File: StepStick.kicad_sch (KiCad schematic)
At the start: 3 parts

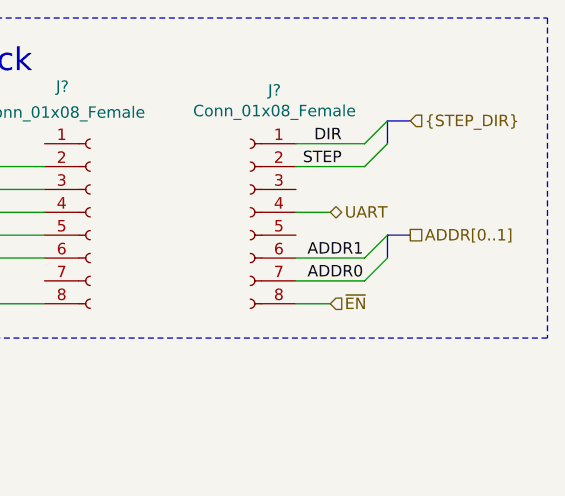
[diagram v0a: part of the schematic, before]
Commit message: Increase text size, redo bus labels
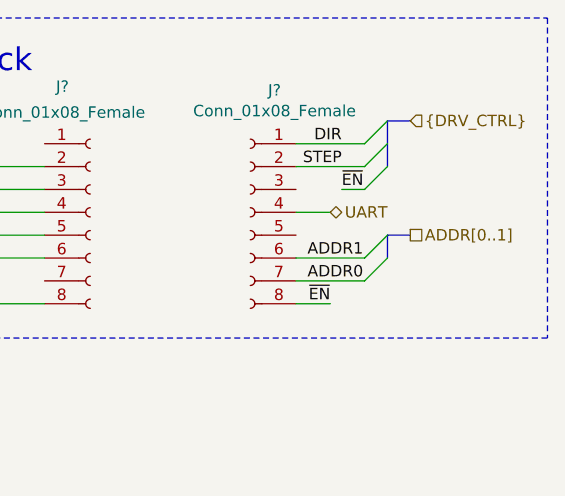
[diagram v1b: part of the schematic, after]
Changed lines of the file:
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@@
-(kicad_sch (version 20200608) (host eeschema "5.99.0-unknown-18ab3c4~101~ubuntu20.04.1")
+(kicad_sch (version 20200608) (host eeschema "5.99.0-unknown-e376750~101~ubuntu20.04.1")
   (page 4 11)
   (paper "A4")
@@
     (comment 1 "Drawn by: Cameron McQuinn")
   )
-  (bus_alias "STEP_DIR" (members "STEP" "DIR"))
+  (bus_alias "DRV_CTRL" (members "STEP" "DIR" "~EN"))
   (bus_entry (at 157.48 77.47) (size 2.54 -2.54))
   (bus_entry (at 157.48 80.01) (size 2.54 -2.54))
+  (bus_entry (at 157.48 82.55) (size 2.54 -2.54))
   (bus_entry (at 157.48 90.17) (size 2.54 -2.54))
   (bus_entry (at 157.48 92.71) (size 2.54 -2.54))
@@
     (stroke (width 0) (type solid) (color 0 0 0 0))
   )
-  (bus (pts (xy 160.02 74.93) (xy 162.56 74.93))
+  (wire (pts (xy 154.94 82.55) (xy 157.48 82.55))
     (stroke (width 0) (type solid) (color 0 0 0 0))
   )
-  (bus (pts (xy 160.02 77.47) (xy 160.02 74.93))
+  (bus (pts (xy 160.02 74.93) (xy 160.02 80.01))
+    (stroke (width 0) (type solid) (color 0 0 0 0))
+  )
+  (bus (pts (xy 160.02 74.93) (xy 162.56 74.93))
     (stroke (width 0) (type solid) (color 0 0 0 0))
   )
@@
     (effects (font (size 1.27 1.27)) (justify left bottom))
   )
+  (label "~EN" (at 153.67 95.25 180)
+    (effects (font (size 1.27 1.27)) (justify right bottom))
+  )
   (label "DIR" (at 154.94 77.47 180)
     (effects (font (size 1.27 1.27)) (justify right bottom))
@@
     (effects (font (size 1.27 1.27)) (justify right bottom))
   )
+  (label "~EN" (at 154.94 82.55 0)
+    (effects (font (size 1.27 1.27)) (justify left bottom))
+  )
   (hierarchical_label "UART" (shape bidirectional) (at 153.67 85.09 0)
     (effects (font (size 1.27 1.27)) (justify left))
   )
-  (hierarchical_label "~EN" (shape input) (at 153.67 95.25 0)
+  (hierarchical_label "{DRV_CTRL}" (shape input) (at 162.56 74.93 0)
     (effects (font (size 1.27 1.27)) (justify left))
   )
-  (hierarchical_label "{STEP_DIR}" (shape input) (at 162.56 74.93 0)
-    (effects (font (size 1.27 1.27)) (justify left))
-  )

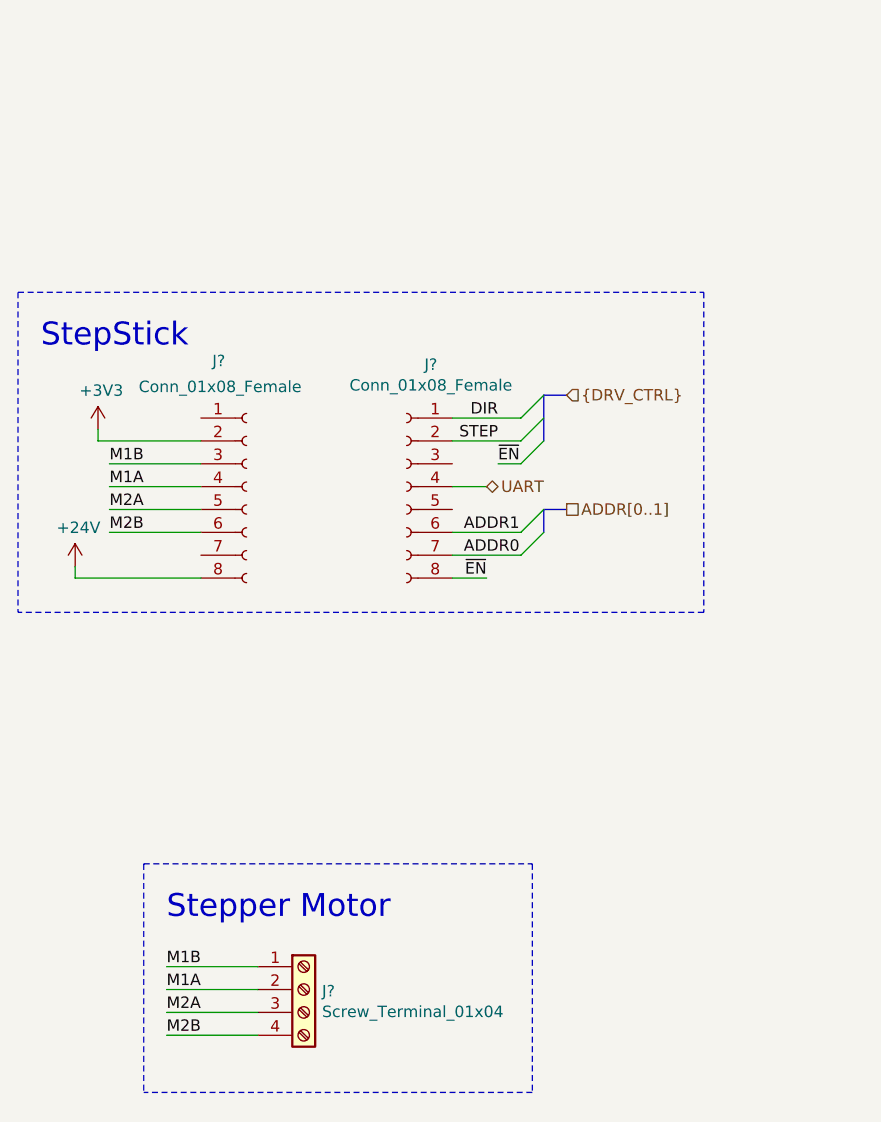
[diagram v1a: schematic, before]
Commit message: Configure driver chip address with jumpers
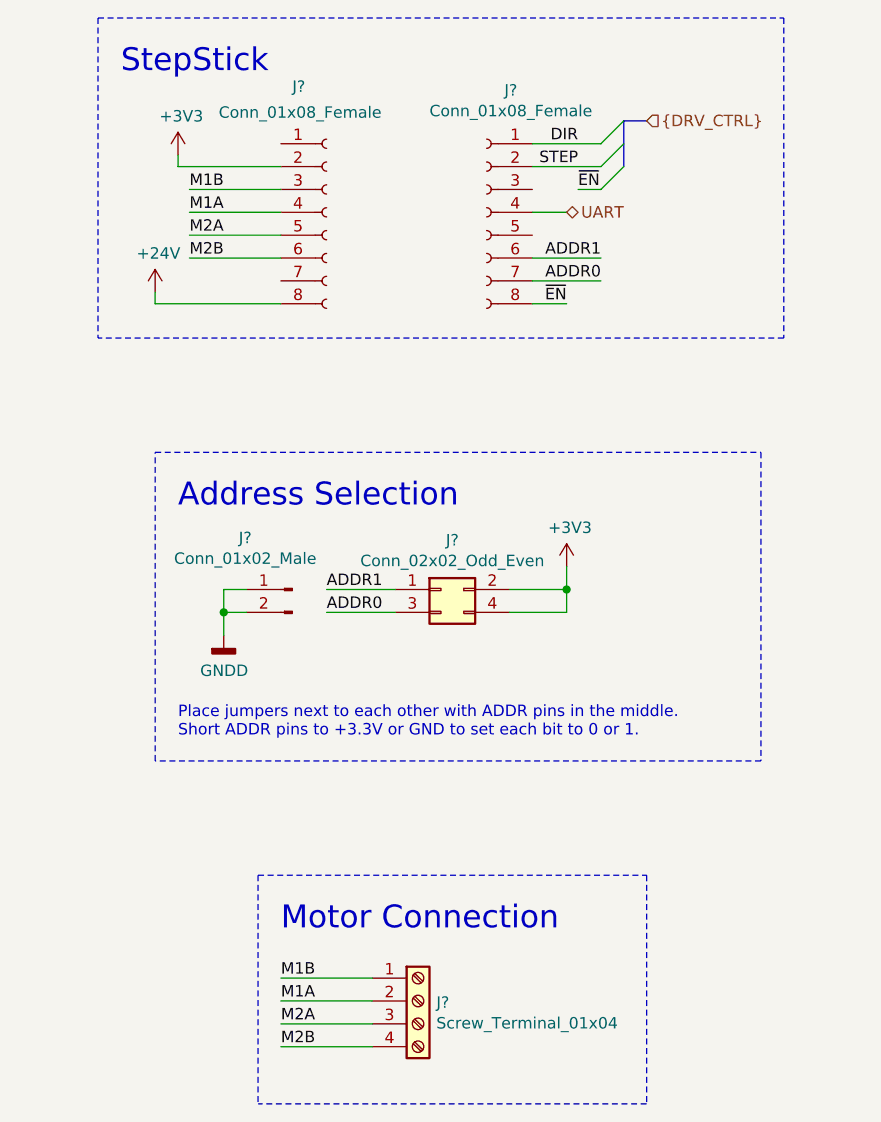
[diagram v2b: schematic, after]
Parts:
- added J?: Conn_01x02_Male, symbol Connector:Conn_01x02_Male
- added J?: Conn_02x02_Odd_Even, symbol Connector_Generic:Conn_02x02_Odd_Even
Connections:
- net +3V3: now also J?.2 (Pin_2), J?.4 (Pin_4)
- net ADDR0: now also J?.3 (Pin_3)
- net ADDR1: now also J?.1 (Pin_1)
- new net GNDD: J?.1 (Pin_1), J?.2 (Pin_2)
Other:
- note added: "Address Selection"
- note added: "Motor Connection"
- note added: "Place jumpers next to each other with ADDR pins in the middle. Short ADDR pins to +3.3V or GND to set each bit to 0 or 1."
- note removed: "Stepper Motor"
- moved on the sheet: J?

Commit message: Annotate schematic
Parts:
- gave numbers to parts that had none: 5
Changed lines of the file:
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@@
-(kicad_sch (version 20200618) (host eeschema "5.99.0-unknown-1463dd1~101~ubuntu20.04.1")
+(kicad_sch (version 20200618) (host eeschema "5.99.0-unknown-77313e4~101~ubuntu20.04.1")
   (page 1 13)
-  (paper "A4")
+  (paper "B")
   (title_block
     (title "StepStick")
@@
   (symbol (lib_id "power:+24V") (at 116.84 63.5 0)
     (in_bom yes) (on_board yes)
-    (property "Reference" "#PWR?" (id 0) (at 116.84 67.31 0)
+    (property "Reference" "#PWR01301" (id 0) (at 116.84 67.31 0)
       (effects (font (size 1.27 1.27)) hide)
     )
@@
   (symbol (lib_id "power:+3V3") (at 119.38 48.26 0)
     (in_bom yes) (on_board yes)
-    (property "Reference" "#PWR?" (id 0) (at 119.38 52.07 0)
+    (property "Reference" "#PWR01302" (id 0) (at 119.38 52.07 0)
       (effects (font (size 1.27 1.27)) hide)
     )
@@
   (symbol (lib_id "power:+3V3") (at 162.56 93.98 0)
     (in_bom yes) (on_board yes)
-    (property "Reference" "#PWR?" (id 0) (at 162.56 97.79 0)
+    (property "Reference" "#PWR01304" (id 0) (at 162.56 97.79 0)
       (effects (font (size 1.27 1.27)) hide)
     )
@@
   (symbol (lib_id "power:GNDD") (at 124.46 101.6 0)
     (in_bom yes) (on_board yes)
-    (property "Reference" "#PWR?" (id 0) (at 124.46 107.95 0)
+    (property "Reference" "#PWR01303" (id 0) (at 124.46 107.95 0)
       (effects (font (size 1.27 1.27)) hide)
     )
@@
   (symbol (lib_id "Connector:Conn_01x02_Male") (at 132.08 96.52 0) (mirror y)
     (in_bom yes) (on_board yes)
-    (property "Reference" "J?" (id 0) (at 126.8476 90.7858 0))
+    (property "Reference" "J1301" (id 0) (at 126.8476 90.7858 0))
     (property "Value" "Conn_01x02_Male" (id 1) (at 126.8476 93.0845 0))
     (property "Footprint" "" (id 2) (at 132.08 96.52 0)
@@
   (symbol (lib_id "Connector:Screw_Terminal_01x04") (at 146.05 142.24 0)
     (in_bom yes) (on_board yes)
-    (property "Reference" "J?" (id 0) (at 148.0821 142.4114 0)
+    (property "Reference" "J1303" (id 0) (at 148.0821 142.4114 0)
       (effects (font (size 1.27 1.27)) (justify left))
     )
@@
   (symbol (lib_id "Connector_Generic:Conn_02x02_Odd_Even") (at 148.59 96.52 0)
     (in_bom yes) (on_board yes)
-    (property "Reference" "J?" (id 0) (at 149.86 91.0398 0))
+    (property "Reference" "J1304" (id 0) (at 149.86 91.0398 0))
     (property "Value" "Conn_02x02_Odd_Even" (id 1) (at 149.86 93.3385 0))
     (property "Footprint" "" (id 2) (at 148.59 96.52 0)
@@
   (symbol (lib_id "Connector:Conn_01x08_Female") (at 135.89 54.61 0)
     (in_bom yes) (on_board yes)
-    (property "Reference" "J?" (id 0) (at 132.08 40.64 0)
+    (property "Reference" "J1302" (id 0) (at 132.08 40.64 0)
       (effects (font (size 1.27 1.27)) (justify left))
     )
@@
   (symbol (lib_id "Connector:Conn_01x08_Female") (at 153.67 54.61 0) (mirror y)
     (in_bom yes) (on_board yes)
-    (property "Reference" "J?" (id 0) (at 156.3624 41.0526 0))
+    (property "Reference" "J1305" (id 0) (at 156.3624 41.0526 0))
     (property "Value" "Conn_01x08_Female" (id 1) (at 156.3624 43.3513 0))
     (property "Footprint" "" (id 2) (at 153.67 54.61 0)

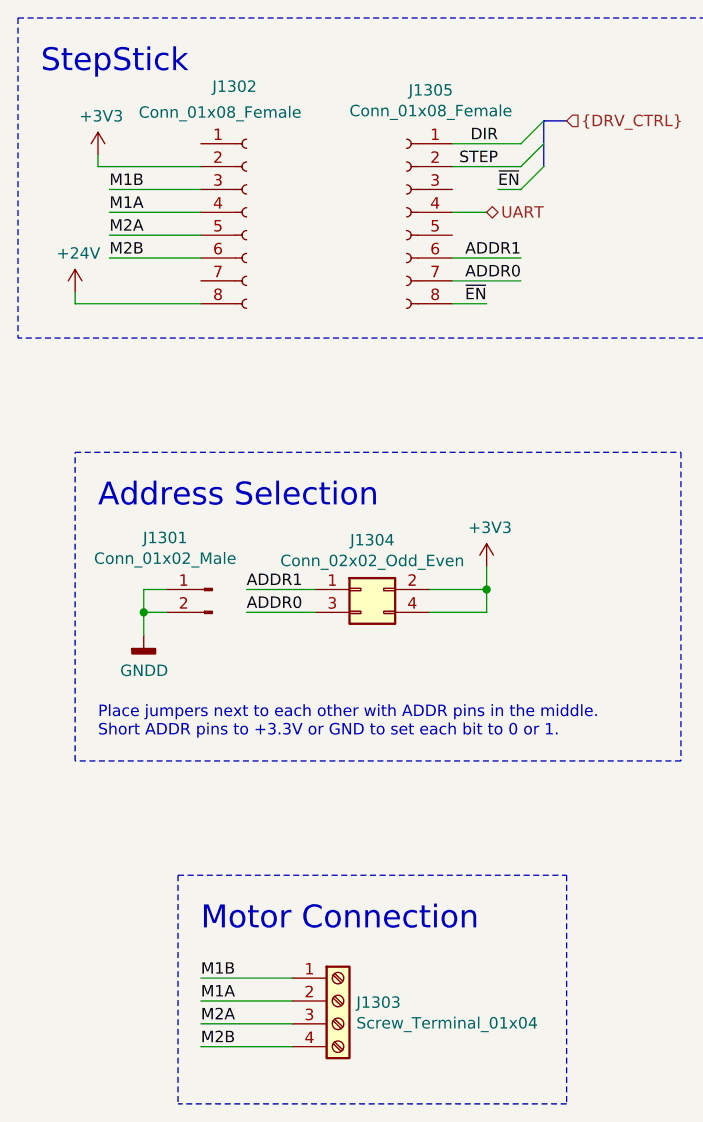
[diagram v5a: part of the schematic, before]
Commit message: Add ULPI USB PHY
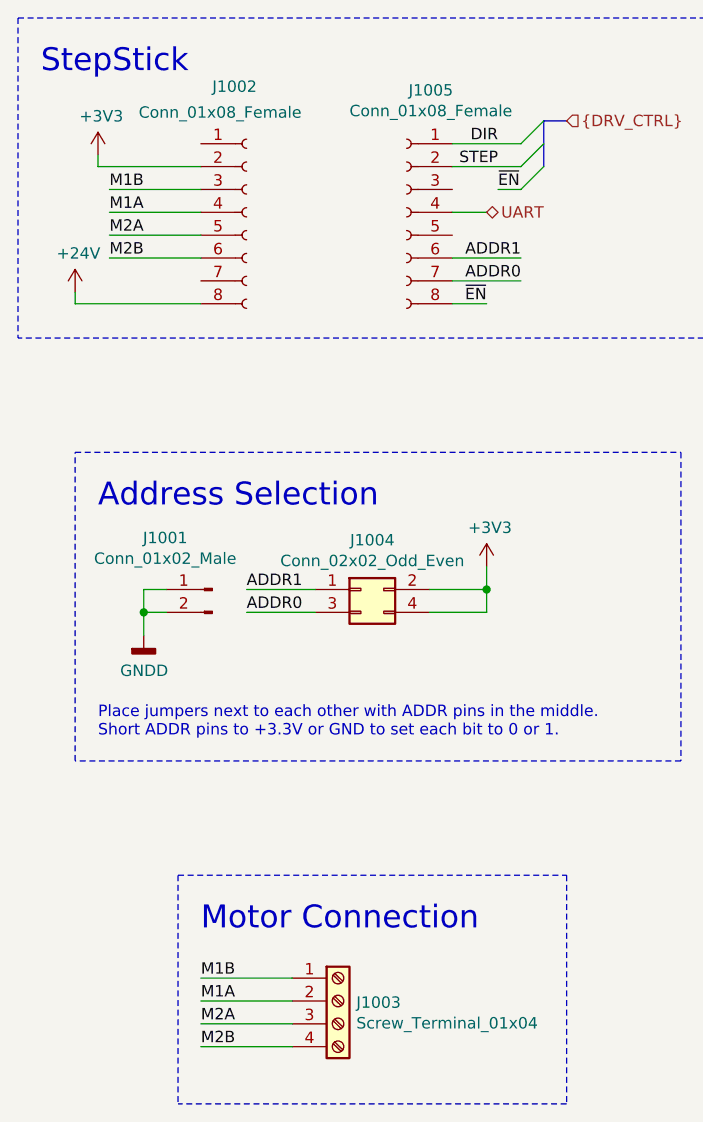
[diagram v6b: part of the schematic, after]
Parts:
- renumbered J1301 to J1001, J1302 to J1002, J1303 to J1003, J1304 to J1004, J1305 to J1005
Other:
- title: StepStick -> StepStick Interface
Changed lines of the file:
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@@
 (kicad_sch (version 20200618) (host eeschema "5.99.0-unknown-77313e4~101~ubuntu20.04.1")
-  (page 1 13)
+  (page 11 14)
   (paper "B")
   (title_block
-    (title "StepStick")
+    (title "StepStick Interface")
     (date "2020-06-24")
     (rev "1.0")
@@
   (symbol (lib_id "power:+24V") (at 116.84 63.5 0)
     (in_bom yes) (on_board yes)
-    (property "Reference" "#PWR01301" (id 0) (at 116.84 67.31 0)
+    (property "Reference" "#PWR01001" (id 0) (at 116.84 67.31 0)
       (effects (font (size 1.27 1.27)) hide)
     )
@@
   (symbol (lib_id "power:+3V3") (at 119.38 48.26 0)
     (in_bom yes) (on_board yes)
-    (property "Reference" "#PWR01302" (id 0) (at 119.38 52.07 0)
+    (property "Reference" "#PWR01002" (id 0) (at 119.38 52.07 0)
       (effects (font (size 1.27 1.27)) hide)
     )
@@
   (symbol (lib_id "power:+3V3") (at 162.56 93.98 0)
     (in_bom yes) (on_board yes)
-    (property "Reference" "#PWR01304" (id 0) (at 162.56 97.79 0)
+    (property "Reference" "#PWR01004" (id 0) (at 162.56 97.79 0)
       (effects (font (size 1.27 1.27)) hide)
     )
@@
   (symbol (lib_id "power:GNDD") (at 124.46 101.6 0)
     (in_bom yes) (on_board yes)
-    (property "Reference" "#PWR01303" (id 0) (at 124.46 107.95 0)
+    (property "Reference" "#PWR01003" (id 0) (at 124.46 107.95 0)
       (effects (font (size 1.27 1.27)) hide)
     )
@@
   (symbol (lib_id "Connector:Conn_01x02_Male") (at 132.08 96.52 0) (mirror y)
     (in_bom yes) (on_board yes)
-    (property "Reference" "J1301" (id 0) (at 126.8476 90.7858 0))
+    (property "Reference" "J1001" (id 0) (at 126.8476 90.7858 0))
     (property "Value" "Conn_01x02_Male" (id 1) (at 126.8476 93.0845 0))
     (property "Footprint" "" (id 2) (at 132.08 96.52 0)
@@
   (symbol (lib_id "Connector:Screw_Terminal_01x04") (at 146.05 142.24 0)
     (in_bom yes) (on_board yes)
-    (property "Reference" "J1303" (id 0) (at 148.0821 142.4114 0)
+    (property "Reference" "J1003" (id 0) (at 148.0821 142.4114 0)
       (effects (font (size 1.27 1.27)) (justify left))
     )
@@
   (symbol (lib_id "Connector_Generic:Conn_02x02_Odd_Even") (at 148.59 96.52 0)
     (in_bom yes) (on_board yes)
-    (property "Reference" "J1304" (id 0) (at 149.86 91.0398 0))
+    (property "Reference" "J1004" (id 0) (at 149.86 91.0398 0))
     (property "Value" "Conn_02x02_Odd_Even" (id 1) (at 149.86 93.3385 0))
     (property "Footprint" "" (id 2) (at 148.59 96.52 0)
@@
   (symbol (lib_id "Connector:Conn_01x08_Female") (at 135.89 54.61 0)
     (in_bom yes) (on_board yes)
-    (property "Reference" "J1302" (id 0) (at 132.08 40.64 0)
+    (property "Reference" "J1002" (id 0) (at 132.08 40.64 0)
       (effects (font (size 1.27 1.27)) (justify left))
     )
@@
   (symbol (lib_id "Connector:Conn_01x08_Female") (at 153.67 54.61 0) (mirror y)
     (in_bom yes) (on_board yes)
-    (property "Reference" "J1305" (id 0) (at 156.3624 41.0526 0))
+    (property "Reference" "J1005" (id 0) (at 156.3624 41.0526 0))
     (property "Value" "Conn_01x08_Female" (id 1) (at 156.3624 43.3513 0))
     (property "Footprint" "" (id 2) (at 153.67 54.61 0)
